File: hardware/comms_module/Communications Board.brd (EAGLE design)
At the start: 54.6 x 32.4 mm, 103 parts, among them U1 Value, U2 STC3115, U3 TCA9554A_PW_16, X2 USB-MICROB, Y1 32.768kHz, Y2 24MHz

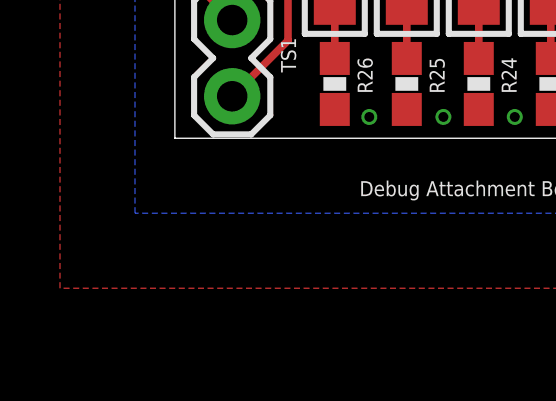
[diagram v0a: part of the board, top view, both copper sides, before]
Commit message: Add extra cap footprint for the 1V3 regulator.
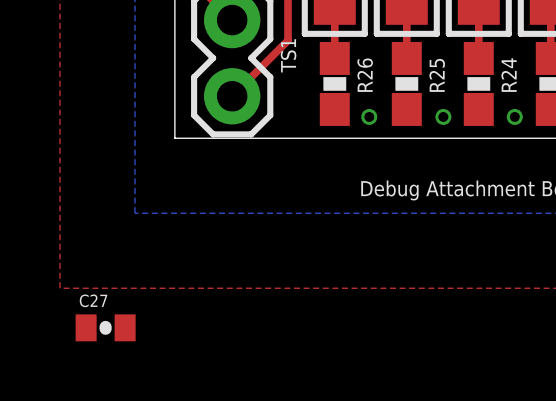
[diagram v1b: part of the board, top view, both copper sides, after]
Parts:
- added C27: DNP, SparkFun-Passives:0402-CAP
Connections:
- net GND: now also C27.2
- net PERIPHERAL_VCC: now also C27.1

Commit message: Fixes from PCB review session.
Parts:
- removed R13: 1Meg, SparkFun-Passives:0603-RES
- removed R16, R18: 100Meg, SparkFun-Passives:0603-RES
- removed R19: 10k, SparkFun-Passives:0603-RES
- removed U$6, U$7: DMC2990UDJ, Capstone Library:SOT963
- added SJ1: (no value), jumper:SJ_2
- R17: value 1M -> DNM
- moved C27 43.3 mm to (35.8, 14.2), flipped to the bottom, turned to 90 degrees
- moved R10 0.42 mm to (13.0, 25.0)
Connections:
- removed net N$12: R13.1, U$6.3
- removed net N$21: R16.2, U$7.6
- removed net N$22: R18.2, R19.2, U$6.4, U$7.2, U$7.5
- removed net N$9: R13.2, U$6.2, U$6.6
- new net N$26: SJ1.2, U2.P9
- net +3V3: now also SJ1.1; no longer R11.2, R12.2, R19.1, U2.P9
- net /SYSDISBL_PF: no longer U$6.5
- net BAT+: no longer R18.1, U$7.4
- net GND: no longer U$6.1, U$7.1
- net PERIPHERAL_VCC: now also R11.2, R12.2, SJ1.3
- net SYSOFF: no longer R16.1, U$7.3
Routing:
- net GND: track 20.4 -> 72.5 mm, vias 129 -> 127
- net N$22: track 15.9 -> 0.00 mm
- net N$9: track 15.6 -> 0.00 mm
- net N$12: track 15.1 -> 0.00 mm
- net +3V3: track 110.8 -> 100.9 mm, vias 7 -> 6
- net N$21: track 6.44 -> 0.00 mm
- net PERIPHERAL_VCC: track 31.2 -> 36.6 mm
- net SYSOFF: track 43.7 -> 43.2 mm
- added copper zone on layer 1, net N$14
- added copper zone on layer 15, net N$14
- added copper zone on layer 16, net N$14
- added copper zone on layer 2, net N$14
- added copper zone on layer 1, net N$25
- added copper zone on layer 15, net N$25
- added copper zone on layer 16, net N$25
- added copper zone on layer 2, net N$25
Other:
- outline, holes or cut-outs redrawn
- board text added: "CUT OUT"

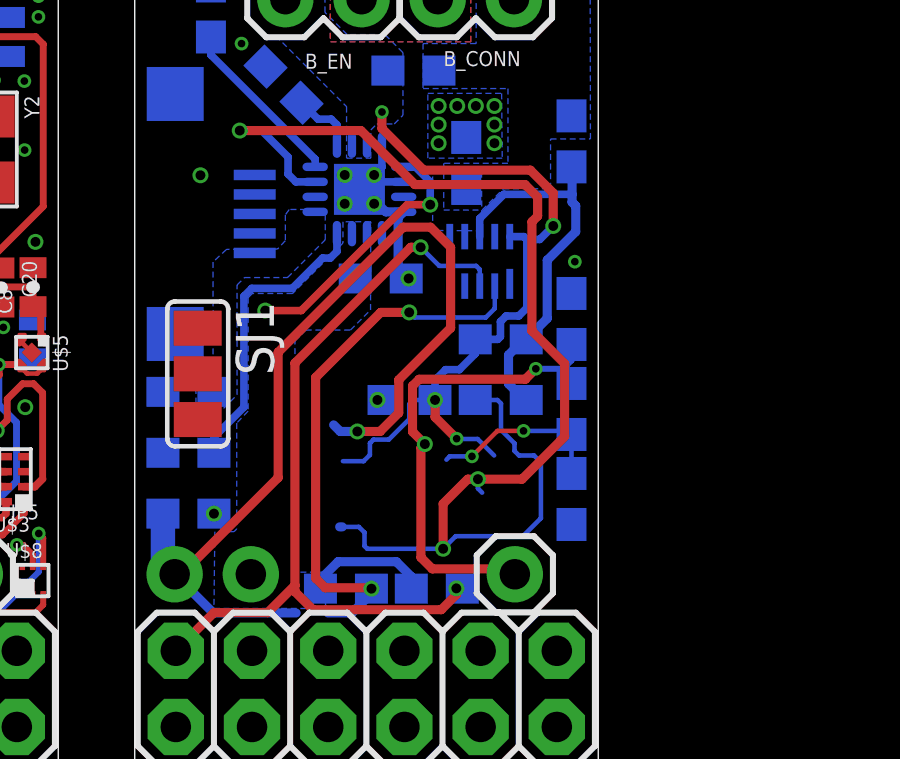
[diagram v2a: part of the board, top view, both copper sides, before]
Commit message: Replace poweroff circuit with NOR gate.
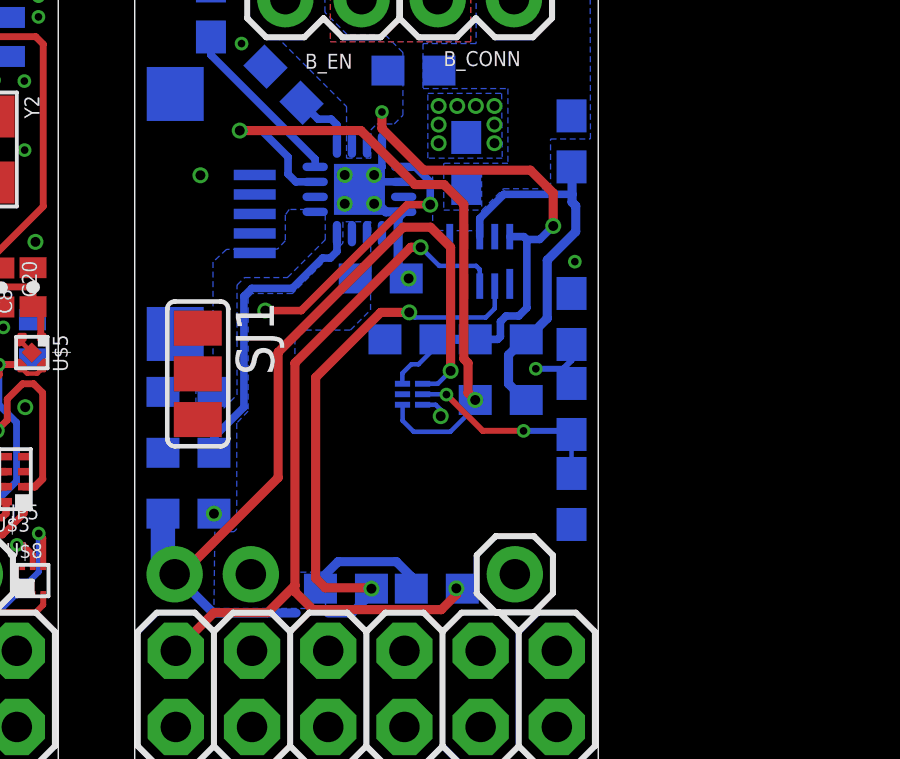
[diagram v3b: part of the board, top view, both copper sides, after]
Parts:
- added U4: SN74AUP1G02_DSF_6, Capstone Library:DSF6
- moved C6 2.02 mm to (48.4, 14.2)
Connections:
- net +3V3: now also U4.1
- net /SYSDISBL_PF: now also U4.2
- net BAT+: now also U4.6
- net GND: now also U4.3
- net SYSOFF: now also U4.4
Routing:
- net SYSOFF: track 43.2 -> 22.6 mm, vias 3 -> 2
- net /SYSDISBL: track 19.7 -> 6.03 mm, vias 2 -> 1
- net BAT+: track 25.0 -> 18.1 mm, vias 4 -> 2
- net +3V3: track 100.9 -> 97.3 mm
- net /SYSDISBL_PF: track 5.92 -> 6.82 mm
- net GND: track 72.5 -> 73.4 mm

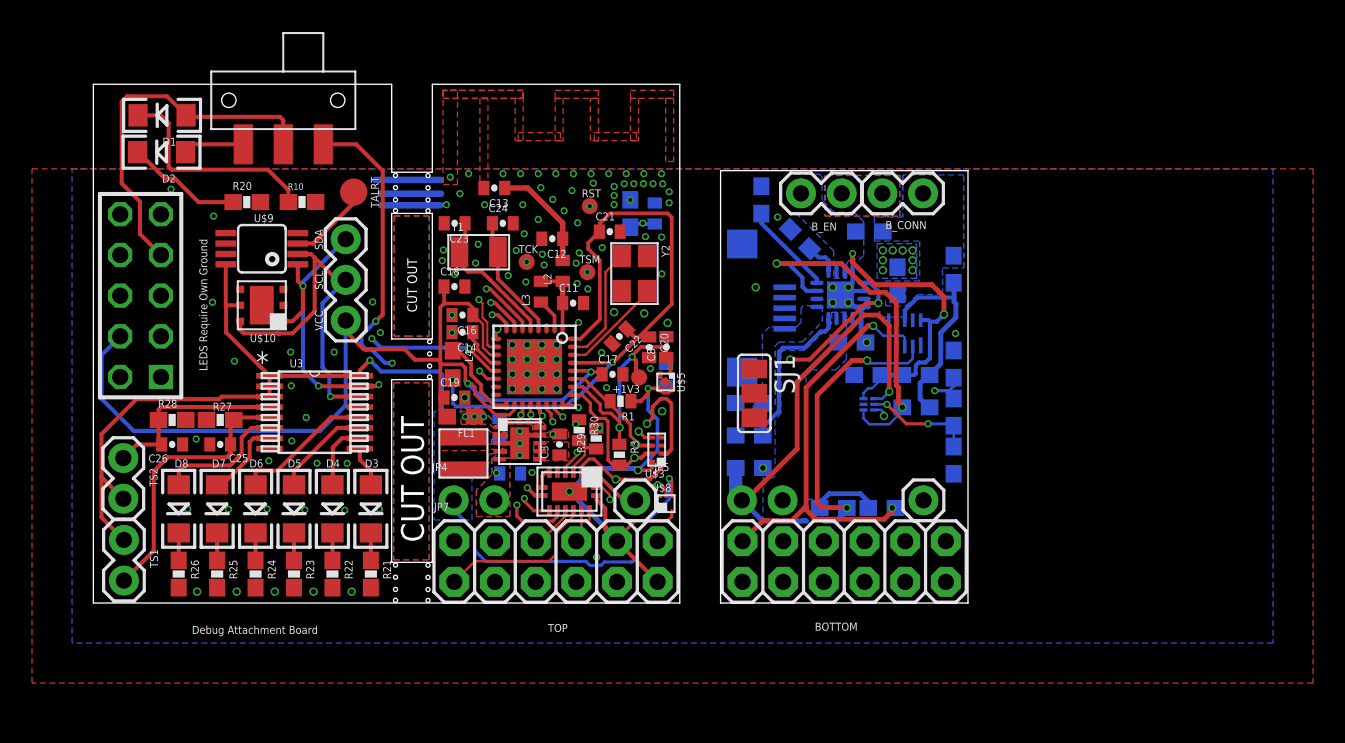
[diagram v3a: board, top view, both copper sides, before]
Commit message: Finish routing of modified boards.
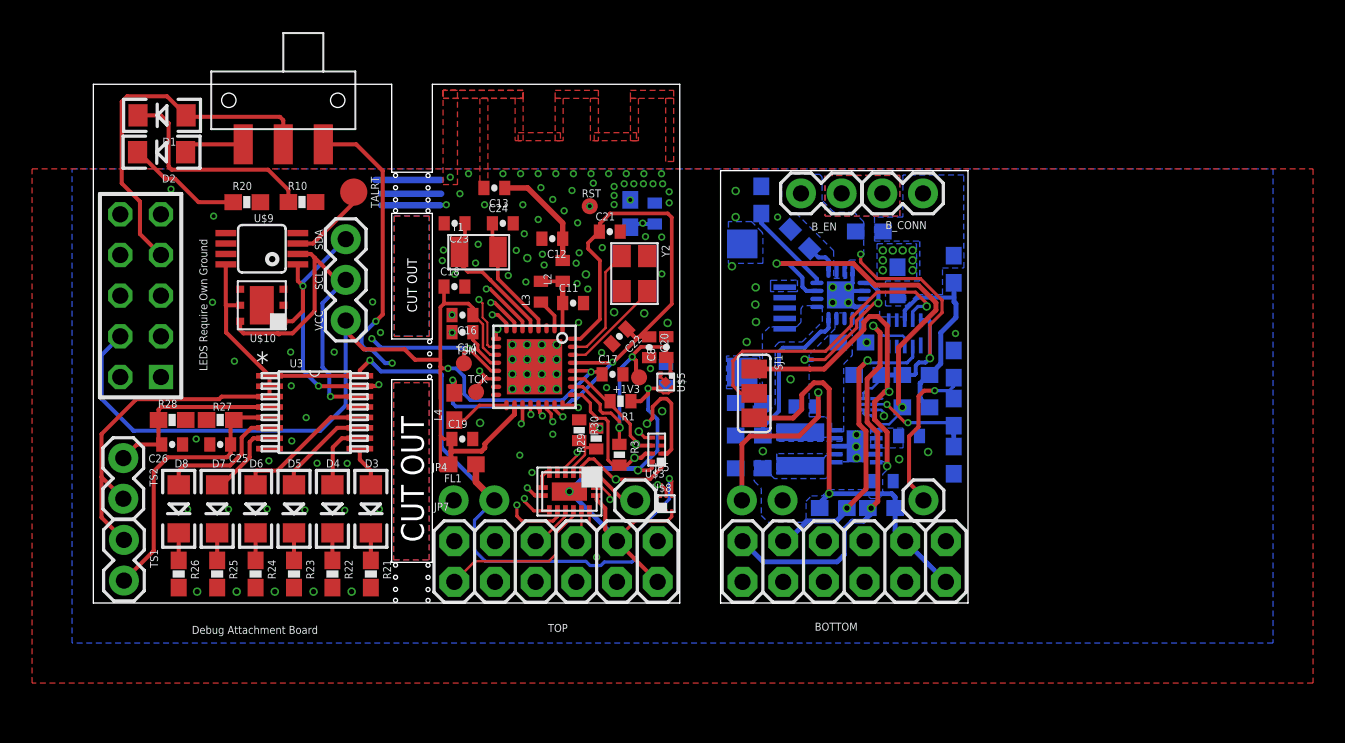
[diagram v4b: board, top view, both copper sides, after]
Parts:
- X2: device SparkFun:USB-MICROB -> Capstone Library:USB-MICROB
- moved C7 24.2 mm to (49.3, 7.61), turned to 180 degrees
- moved C3 21.8 mm to (50.9, 10.4), flipped to the bottom, turned to 180 degrees
- moved L1 21.0 mm to (44.1, 9.62), flipped to the bottom, turned to 270 degrees
- moved U$4 21.0 mm to (47.6, 9.79), flipped to the bottom, turned to 90 degrees
- moved C1 18.8 mm to (44.4, 12.3), turned to 0 degrees
- moved TSM 9.58 mm to (23.1, 15.0)
- moved TCK 8.71 mm to (23.9, 13.2)
- moved FL1 2.98 mm to (23.0, 8.66)
- moved C19 2.64 mm to (23.0, 10.2)
- moved L4 2.63 mm to (22.5, 12.3), turned to 90 degrees
- turned R11 to 180 degrees
- turned C10 to 0 degrees
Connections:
- net +3V3: now also JP3.2, JP4.2; no longer JP3.1, JP4.1
- net GND: now also X2.MT1, X2.MT2
- net V_PREBUCK: now also JP3.1, JP4.1; no longer JP3.2, JP4.2
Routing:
- net PERIPHERAL_VCC: track 36.6 -> 57.2 mm, vias 3 -> 4
- net N$26: track 0.00 -> 19.2 mm, vias 0 -> 1
- net V_PREBUCK: track 48.7 -> 60.4 mm
- net /SYSDISBL: track 6.03 -> 14.3 mm
- net VCC: track 81.1 -> 88.2 mm
- net SYSOFF: track 22.6 -> 25.9 mm
- net DCDC_SW: track 5.58 -> 3.65 mm
- net JTAG_TSMC: track 34.8 -> 33.0 mm, vias 3 -> 2
- net BAT+: track 18.1 -> 19.2 mm
- net +3V3: track 97.3 -> 96.2 mm, vias 6 -> 4
- net JTAG_TCKC: track 31.8 -> 30.8 mm, vias 2 -> 1
- net VDDR: track 41.8 -> 42.6 mm
- net MCU_RST: track 56.9 -> 57.7 mm
- net GND: track 73.4 -> 73.2 mm, vias 127 -> 138
- added copper zone on layer 16, net N$10
- added copper zone on layer 16, net N$5
- added copper zone on layer 16, net N$8
- removed copper zone on layer 1, net +3V3
- removed copper zone on layer 1, net N$10
- removed copper zone on layer 1, net N$5
- removed copper zone on layer 1, net N$8
- removed copper zone on layer 1, net V_PREBUCK

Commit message: Adding final version before split.
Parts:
- moved R30 0.96 mm to (29.6, 10.2)
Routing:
- net PERIPHERAL_DETECT: track 9.96 -> 8.76 mm
- net V_PREBUCK_DIV2: track 3.19 -> 3.76 mm
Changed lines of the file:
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@@
 <attribute name="VALUE" x="32.543" y="9.1905" size="0.5" layer="27" ratio="11" rot="R90"/>
 </element>
-<element name="R30" library="SparkFun-Passives" package="0402-RES" value="1Meg" x="30.34" y="10.79" smashed="yes" rot="R270">
-<attribute name="NAME" x="31.0385" y="11.679" size="0.5" layer="25" ratio="11" rot="R270"/>
+<element name="R30" library="SparkFun-Passives" package="0402-RES" value="1Meg" x="29.57" y="10.21" smashed="yes" rot="R270">
+<attribute name="NAME" x="30.2685" y="11.099" size="0.5" layer="25" ratio="11" rot="R270"/>
 </element>
 <element name="C27" library="SparkFun-Passives" package="0402-CAP" value="DNP" x="35.76" y="14.24" smashed="yes" rot="MR90">
@@
 <via x="22.41" y="16.88" extent="1-16" drill="0.254"/>
 <via x="24.15" y="11.25" extent="1-16" drill="0.3302"/>
-<via x="28.69" y="10.54" extent="1-16" drill="0.254"/>
+<via x="28.56" y="10.23" extent="1-16" drill="0.254"/>
 <via x="25.91" y="20.45" extent="1-16" drill="0.254"/>
 <via x="27.01" y="20.05" extent="1-16" drill="0.254"/>
@@
 <wire x1="32.88" y1="5.52" x2="32.25" y2="5.52" width="0.1524" layer="15"/>
 <wire x1="32.25" y1="5.52" x2="31.07" y2="6.7" width="0.1524" layer="15"/>
-<wire x1="31.07" y1="6.7" x2="31.07" y2="8.55" width="0.1524" layer="15"/>
-<via x="30.21" y="9.41" extent="1-16" drill="0.254"/>
-<wire x1="29.48" y1="8.16" x2="29.48" y2="8.49" width="0.1524" layer="1"/>
-<wire x1="30.21" y1="9.22" x2="30.21" y2="9.41" width="0.1524" layer="1"/>
-<wire x1="29.48" y1="8.49" x2="30.21" y2="9.22" width="0.1524" layer="1"/>
-<wire x1="31.07" y1="8.55" x2="30.21" y2="9.41" width="0.1524" layer="15"/>
+<via x="29.49" y="8.81" extent="1-16" drill="0.254"/>
+<wire x1="29.48" y1="8.16" x2="29.48" y2="8.8" width="0.1524" layer="1"/>
+<wire x1="31.07" y1="6.7" x2="31.07" y2="7.23" width="0.1524" layer="15"/>
+<wire x1="31.07" y1="7.23" x2="29.49" y2="8.81" width="0.1524" layer="15"/>
+<wire x1="29.48" y1="8.8" x2="29.49" y2="8.81" width="0.1524" layer="1"/>
 <wire x1="35.24" y1="3.86" x2="53.24" y2="3.86" width="0" layer="19" extent="1-1"/>
 </signal>
@@
 <wire x1="29.98" y1="8.53" x2="30.7" y2="9.25" width="0.1524" layer="1"/>
 <wire x1="30.7" y1="9.25" x2="30.7" y2="9.7" width="0.1524" layer="1"/>
-<wire x1="30.7" y1="9.7" x2="30.37" y2="10.03" width="0.1524" layer="1"/>
-<wire x1="30.37" y1="10.03" x2="30.22" y2="10.03" width="0.1524" layer="1"/>
 <contactref element="R29" pad="1"/>
 <contactref element="R30" pad="2"/>
 <wire x1="31.4" y1="9.62" x2="31.32" y2="9.7" width="0.2" layer="1"/>
 <wire x1="31.32" y1="9.7" x2="30.7" y2="9.7" width="0.2" layer="1"/>
-<wire x1="30.34" y1="10.14" x2="30.37" y2="10.03" width="0" layer="19" extent="1-1"/>
+<wire x1="30.7" y1="9.7" x2="29.71" y2="9.7" width="0.2" layer="1"/>
+<wire x1="29.71" y1="9.7" x2="29.57" y2="9.56" width="0.2" layer="1"/>
 </signal>
 <signal name="N$14">
